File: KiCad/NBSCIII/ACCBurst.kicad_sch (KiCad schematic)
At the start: 56 parts, among them Q901 BC337-25, Q902 BC337-25, Q903 BC337-25, Q910 BC337-25, Q911 BC337-25, Q912 BC337-25, U1 LM324N

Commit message: unrescue Device:D
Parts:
- D901, D902, D930: symbol NBSCIII-rescue:DIODE -> Device:D
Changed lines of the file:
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@@
   (junction (at 238.76 87.63) (diameter 0) (color 0 0 0 0)
   )
+  (junction (at 204.47 129.54) (diameter 0) (color 0 0 0 0)
+  )
+  (junction (at 180.34 113.03) (diameter 0) (color 0 0 0 0)
+  )
+  (junction (at 118.11 25.4) (diameter 0) (color 0 0 0 0)
+  )
+  (junction (at 49.53 105.41) (diameter 0) (color 0 0 0 0)
+  )
+  (junction (at 148.59 129.54) (diameter 0) (color 0 0 0 0)
+  )
+  (junction (at 167.64 87.63) (diameter 0) (color 0 0 0 0)
+  )
+  (junction (at 29.21 129.54) (diameter 0) (color 0 0 0 0)
+  )
   (junction (at 227.33 116.84) (diameter 0) (color 0 0 0 0)
   )
-  (junction (at 204.47 129.54) (diameter 0) (color 0 0 0 0)
-  )
-  (junction (at 180.34 113.03) (diameter 0) (color 0 0 0 0)
-  )
-  (junction (at 118.11 25.4) (diameter 0) (color 0 0 0 0)
-  )
-  (junction (at 49.53 105.41) (diameter 0) (color 0 0 0 0)
-  )
-  (junction (at 148.59 129.54) (diameter 0) (color 0 0 0 0)
-  )
-  (junction (at 167.64 87.63) (diameter 0) (color 0 0 0 0)
-  )
-  (junction (at 29.21 129.54) (diameter 0) (color 0 0 0 0)
-  )
   (junction (at 64.77 25.4) (diameter 0) (color 0 0 0 0)
   )
@@
     (stroke (width 0) (type default) (color 0 0 0 0))
   )
-  (wire (pts (xy 243.84 142.24) (xy 264.16 142.24))
+  (wire (pts (xy 242.57 142.24) (xy 264.16 142.24))
     (stroke (width 0) (type default) (color 0 0 0 0))
   )
@@
     (stroke (width 0) (type default) (color 0 0 0 0))
   )
-  (wire (pts (xy 227.33 106.68) (xy 227.33 105.41))
-    (stroke (width 0) (type default) (color 0 0 0 0))
-  )
   (wire (pts (xy 227.33 105.41) (xy 205.74 105.41))
     (stroke (width 0) (type default) (color 0 0 0 0))
@@
     (stroke (width 0) (type default) (color 0 0 0 0))
   )
-  (wire (pts (xy 102.87 142.24) (xy 233.68 142.24))
+  (wire (pts (xy 102.87 142.24) (xy 234.95 142.24))
     (stroke (width 0) (type default) (color 0 0 0 0))
   )
@@
     (stroke (width 0) (type default) (color 0 0 0 0))
   )
-  (wire (pts (xy 180.34 67.31) (xy 180.34 72.39))
+  (wire (pts (xy 180.34 66.04) (xy 180.34 72.39))
     (stroke (width 0) (type default) (color 0 0 0 0))
   )
@@
     (stroke (width 0) (type default) (color 0 0 0 0))
   )
+  (wire (pts (xy 227.33 105.41) (xy 227.33 107.95))
+    (stroke (width 0) (type default) (color 0 0 0 0))
+  )
   (wire (pts (xy 102.87 129.54) (xy 68.58 129.54))
     (stroke (width 0) (type default) (color 0 0 0 0))
@@
     (stroke (width 0) (type default) (color 0 0 0 0))
   )
-  (wire (pts (xy 180.34 39.37) (xy 180.34 57.15))
+  (wire (pts (xy 180.34 39.37) (xy 180.34 58.42))
     (stroke (width 0) (type default) (color 0 0 0 0))
   )
@@
     (stroke (width 0) (type default) (color 0 0 0 0))
   )
+  (wire (pts (xy 227.33 116.84) (xy 231.14 116.84))
+    (stroke (width 0) (type default) (color 0 0 0 0))
+  )
   (wire (pts (xy 49.53 120.65) (xy 49.53 129.54))
     (stroke (width 0) (type default) (color 0 0 0 0))
@@
     (stroke (width 0) (type default) (color 0 0 0 0))
   )
+  (wire (pts (xy 227.33 115.57) (xy 227.33 116.84))
+    (stroke (width 0) (type default) (color 0 0 0 0))
+  )
   (polyline (pts (xy 22.86 88.9) (xy 22.86 132.08))
     (stroke (width 0) (type default) (color 0 0 0 0))
@@
   )
   (polyline (pts (xy 232.41 147.32) (xy 232.41 86.36))
-    (stroke (width 0) (type default) (color 0 0 0 0))
-  )
-  (wire (pts (xy 227.33 116.84) (xy 231.14 116.84))
     (stroke (width 0) (type default) (color 0 0 0 0))
   )
@@
     (pin "2")
   )
-  (symbol (lib_id "NBSCIII-rescue:DIODE") (at 180.34 62.23 270) (unit 1)
+  (symbol (lib_id "Device:D") (at 180.34 62.23 270) (unit 1)
     (in_bom yes) (on_board yes)
     (property "Reference" "D901" (id 0) (at 182.88 62.23 0)
@@
     (pin "2")
   )
-  (symbol (lib_id "NBSCIII-rescue:DIODE") (at 227.33 111.76 90) (unit 1)
+  (symbol (lib_id "Device:D") (at 227.33 111.76 90) (unit 1)
     (in_bom yes) (on_board yes)
     (property "Reference" "D902" (id 0) (at 224.79 111.76 0)
@@
     (pin "2")
   )
-  (symbol (lib_id "NBSCIII-rescue:DIODE") (at 238.76 142.24 0) (unit 1)
+  (symbol (lib_id "Device:D") (at 238.76 142.24 0) (unit 1)
     (in_bom yes) (on_board yes)
     (property "Reference" "D930" (id 0) (at 238.76 139.7 0)

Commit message: unrescue Device:L_small
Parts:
- L910, L911: symbol NBSCIII-rescue:INDUCTOR -> Device:L_Small
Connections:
- net VIDEO renamed video
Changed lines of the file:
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@@
     (stroke (width 0) (type default) (color 0 0 0 0))
   )
-  (wire (pts (xy 41.91 109.22) (xy 41.91 105.41))
+  (wire (pts (xy 41.91 105.41) (xy 41.91 114.3))
     (stroke (width 0) (type default) (color 0 0 0 0))
   )
@@
     (stroke (width 0) (type default) (color 0 0 0 0))
   )
-  (wire (pts (xy 41.91 129.54) (xy 41.91 124.46))
+  (wire (pts (xy 41.91 119.38) (xy 41.91 129.54))
     (stroke (width 0) (type default) (color 0 0 0 0))
   )
@@
     (stroke (width 0) (type default) (color 0 0 0 0))
   )
-  (wire (pts (xy 185.42 87.63) (xy 185.42 88.9))
+  (wire (pts (xy 185.42 87.63) (xy 185.42 93.98))
     (stroke (width 0) (type default) (color 0 0 0 0))
   )
@@
     (stroke (width 0) (type default) (color 0 0 0 0))
   )
-  (wire (pts (xy 185.42 104.14) (xy 185.42 105.41))
+  (wire (pts (xy 185.42 99.06) (xy 185.42 105.41))
     (stroke (width 0) (type default) (color 0 0 0 0))
   )
@@
     (effects (font (size 1.524 1.524)) (justify right))
   )
-  (hierarchical_label "VIDEO" (shape input) (at 22.86 92.71 180)
+  (hierarchical_label "video" (shape input) (at 22.86 92.71 180)
     (effects (font (size 1.524 1.524)) (justify right))
   )
@@
     (pin "2")
   )
-  (symbol (lib_id "NBSCIII-rescue:INDUCTOR") (at 41.91 116.84 0) (unit 1)
+  (symbol (lib_id "Device:L_Small") (at 41.91 116.84 0) (unit 1)
     (in_bom yes) (on_board yes)
     (property "Reference" "L910" (id 0) (at 40.64 116.84 90)
@@
     (pin "2")
   )
-  (symbol (lib_id "NBSCIII-rescue:INDUCTOR") (at 185.42 96.52 0) (unit 1)
+  (symbol (lib_id "Device:L_Small") (at 185.42 96.52 0) (unit 1)
     (in_bom yes) (on_board yes)
     (property "Reference" "L911" (id 0) (at 184.15 96.52 90)

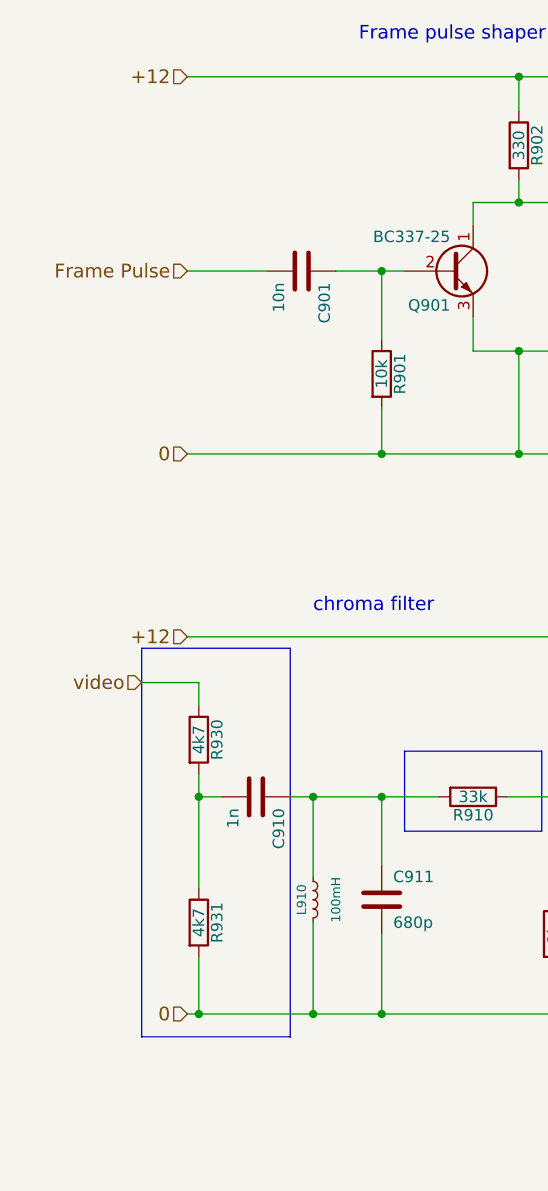
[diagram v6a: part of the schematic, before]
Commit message: Simplify power distribution and make global
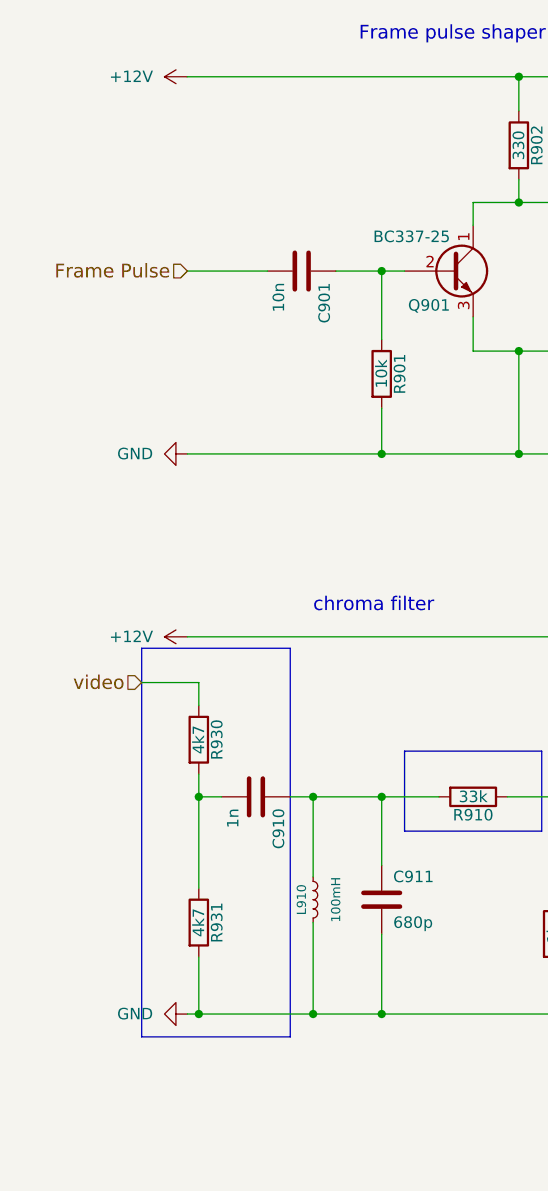
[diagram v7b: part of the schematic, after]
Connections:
- net +12 renamed +12V
- net 0 renamed GND
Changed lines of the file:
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@@
     (effects (font (size 1.524 1.524)) (justify left bottom))
-  )
-  (hierarchical_label "+12" (shape input) (at 27.94 87.63 180)
-    (effects (font (size 1.524 1.524)) (justify right))
   )
   (hierarchical_label "C" (shape output) (at 162.56 135.89 0)
     (effects (font (size 1.524 1.524)) (justify left))
   )
-  (hierarchical_label "0" (shape input) (at 27.94 129.54 180)
-    (effects (font (size 1.524 1.524)) (justify right))
-  )
   (hierarchical_label "Frame Pulse" (shape input) (at 27.94 46.99 180)
     (effects (font (size 1.524 1.524)) (justify right))
   )
-  (hierarchical_label "+12" (shape input) (at 27.94 25.4 180)
-    (effects (font (size 1.524 1.524)) (justify right))
-  )
   (hierarchical_label "BURST" (shape output) (at 231.14 105.41 0)
     (effects (font (size 1.524 1.524)) (justify left))
-  )
-  (hierarchical_label "0" (shape input) (at 27.94 67.31 180)
-    (effects (font (size 1.524 1.524)) (justify right))
   )
   (hierarchical_label "video" (shape input) (at 22.86 92.71 180)
@@
     (pin "2")
   )
+  (symbol (lib_id "power:+12V") (at 27.94 87.63 90) (unit 1)
+    (in_bom yes) (on_board yes) (fields_autoplaced)
+    (property "Reference" "#PWR0121" (id 0) (at 31.75 87.63 0)
+      (effects (font (size 1.27 1.27)) hide)
+    )
+    (property "Value" "+12V" (id 1) (at 24.13 87.6299 90)
+      (effects (font (size 1.27 1.27)) (justify left))
+    )
+    (property "Footprint" "" (id 2) (at 27.94 87.63 0)
+      (effects (font (size 1.27 1.27)) hide)
+    )
+    (property "Datasheet" "" (id 3) (at 27.94 87.63 0)
+      (effects (font (size 1.27 1.27)) hide)
+    )
+    (pin "1")
+  )
+  (symbol (lib_id "power:GND") (at 27.94 129.54 270) (unit 1)
+    (in_bom yes) (on_board yes) (fields_autoplaced)
+    (property "Reference" "#PWR0120" (id 0) (at 21.59 129.54 0)
+      (effects (font (size 1.27 1.27)) hide)
+    )
+    (property "Value" "GND" (id 1) (at 24.13 129.5399 90)
+      (effects (font (size 1.27 1.27)) (justify right))
+    )
+    (property "Footprint" "" (id 2) (at 27.94 129.54 0)
+      (effects (font (size 1.27 1.27)) hide)
+    )
+    (property "Datasheet" "" (id 3) (at 27.94 129.54 0)
+      (effects (font (size 1.27 1.27)) hide)
+    )
+    (pin "1")
+  )
+  (symbol (lib_id "power:+12V") (at 27.94 25.4 90) (unit 1)
+    (in_bom yes) (on_board yes) (fields_autoplaced)
+    (property "Reference" "#PWR0119" (id 0) (at 31.75 25.4 0)
+      (effects (font (size 1.27 1.27)) hide)
+    )
+    (property "Value" "+12V" (id 1) (at 24.13 25.3999 90)
+      (effects (font (size 1.27 1.27)) (justify left))
+    )
+    (property "Footprint" "" (id 2) (at 27.94 25.4 0)
+      (effects (font (size 1.27 1.27)) hide)
+    )
+    (property "Datasheet" "" (id 3) (at 27.94 25.4 0)
+      (effects (font (size 1.27 1.27)) hide)
+    )
+    (pin "1")
+  )
+  (symbol (lib_id "power:GND") (at 27.94 67.31 270) (unit 1)
+    (in_bom yes) (on_board yes) (fields_autoplaced)
+    (property "Reference" "#PWR0118" (id 0) (at 21.59 67.31 0)
+      (effects (font (size 1.27 1.27)) hide)
+    )
+    (property "Value" "GND" (id 1) (at 24.13 67.3099 90)
+      (effects (font (size 1.27 1.27)) (justify right))
+    )
+    (property "Footprint" "" (id 2) (at 27.94 67.31 0)
+      (effects (font (size 1.27 1.27)) hide)
+    )
+    (property "Datasheet" "" (id 3) (at 27.94 67.31 0)
+      (effects (font (size 1.27 1.27)) hide)
+    )
+    (pin "1")
+  )
 )

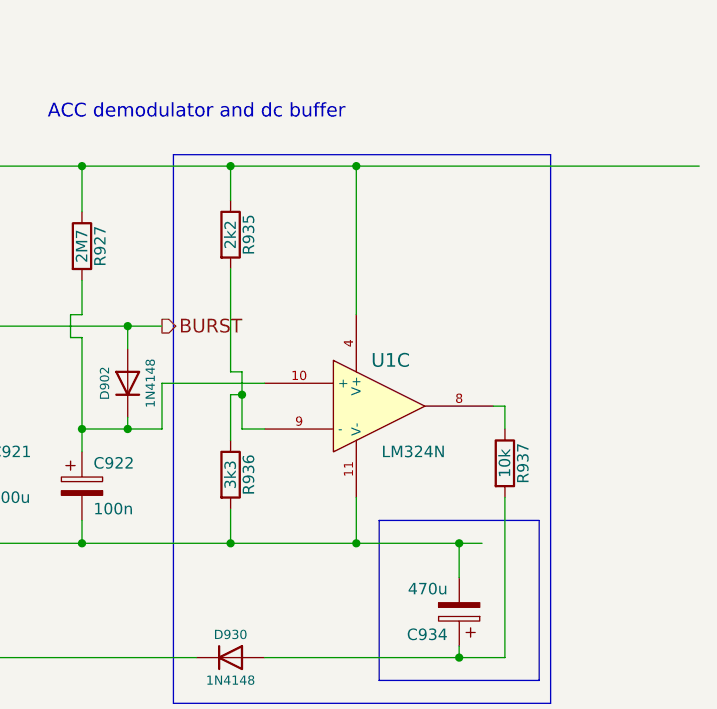
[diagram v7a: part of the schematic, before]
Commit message: derescue lm324
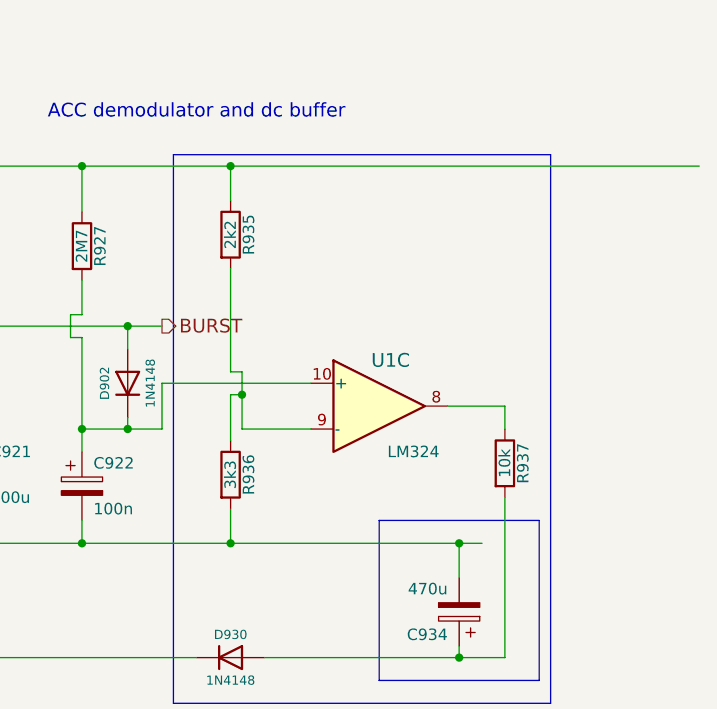
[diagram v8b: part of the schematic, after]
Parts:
- U1: value LM324N -> LM324; symbol NBSCIII-rescue:LM324N -> Amplifier_Operational:LM324
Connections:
- net +12V: no longer U1.4 (V+)
- net GND: no longer U1.11 (V-)
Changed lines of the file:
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@@
   (junction (at 210.82 129.54) (diameter 0) (color 0 0 0 0)
   )
-  (junction (at 252.73 87.63) (diameter 0) (color 0 0 0 0)
-  )
   (junction (at 204.47 114.3) (diameter 0) (color 0 0 0 0)
   )
@@
   (junction (at 130.81 102.87) (diameter 0) (color 0 0 0 0)
   )
-  (junction (at 252.73 129.54) (diameter 0) (color 0 0 0 0)
-  )
   (junction (at 146.05 104.14) (diameter 0) (color 0 0 0 0)
   )
@@
     (stroke (width 0) (type default) (color 0 0 0 0))
   )
-  (wire (pts (xy 231.14 111.76) (xy 242.57 111.76))
-    (stroke (width 0) (type default) (color 0 0 0 0))
-  )
   (wire (pts (xy 41.91 105.41) (xy 49.53 105.41))
     (stroke (width 0) (type default) (color 0 0 0 0))
@@
     (stroke (width 0) (type default) (color 0 0 0 0))
   )
-  (wire (pts (xy 267.97 114.3) (xy 269.24 114.3))
+  (wire (pts (xy 262.89 114.3) (xy 269.24 114.3))
     (stroke (width 0) (type default) (color 0 0 0 0))
   )
@@
     (stroke (width 0) (type default) (color 0 0 0 0))
   )
-  (wire (pts (xy 252.73 129.54) (xy 238.76 129.54))
+  (wire (pts (xy 238.76 129.54) (xy 264.16 129.54))
     (stroke (width 0) (type default) (color 0 0 0 0))
   )
@@
     (stroke (width 0) (type default) (color 0 0 0 0))
   )
-  (wire (pts (xy 264.16 129.54) (xy 252.73 129.54))
-    (stroke (width 0) (type default) (color 0 0 0 0))
-  )
   (wire (pts (xy 180.34 111.76) (xy 176.53 111.76))
     (stroke (width 0) (type default) (color 0 0 0 0))
@@
     (stroke (width 0) (type default) (color 0 0 0 0))
   )
+  (wire (pts (xy 240.03 116.84) (xy 247.65 116.84))
+    (stroke (width 0) (type default) (color 0 0 0 0))
+  )
   (polyline (pts (xy 115.57 30.48) (xy 77.47 30.48))
     (stroke (width 0) (type default) (color 0 0 0 0))
   )
+  (wire (pts (xy 231.14 111.76) (xy 247.65 111.76))
+    (stroke (width 0) (type default) (color 0 0 0 0))
+  )
   (wire (pts (xy 156.21 104.14) (xy 158.75 104.14))
     (stroke (width 0) (type default) (color 0 0 0 0))
@@
     (stroke (width 0) (type default) (color 0 0 0 0))
   )
-  (wire (pts (xy 242.57 116.84) (xy 240.03 116.84))
-    (stroke (width 0) (type default) (color 0 0 0 0))
-  )
   (wire (pts (xy 264.16 129.54) (xy 264.16 133.35))
     (stroke (width 0) (type default) (color 0 0 0 0))
@@
     (stroke (width 0) (type default) (color 0 0 0 0))
   )
-  (wire (pts (xy 252.73 87.63) (xy 290.83 87.63))
+  (wire (pts (xy 238.76 87.63) (xy 290.83 87.63))
     (stroke (width 0) (type default) (color 0 0 0 0))
   )
@@
     (stroke (width 0) (type default) (color 0 0 0 0))
   )
-  (wire (pts (xy 252.73 124.46) (xy 252.73 129.54))
-    (stroke (width 0) (type default) (color 0 0 0 0))
-  )
   (wire (pts (xy 118.11 52.07) (xy 118.11 67.31))
     (stroke (width 0) (type default) (color 0 0 0 0))
@@
     (stroke (width 0) (type default) (color 0 0 0 0))
   )
-  (wire (pts (xy 252.73 104.14) (xy 252.73 87.63))
-    (stroke (width 0) (type default) (color 0 0 0 0))
-  )
   (wire (pts (xy 85.09 130.81) (xy 85.09 128.27))
     (stroke (width 0) (type default) (color 0 0 0 0))
@@
   )
   (wire (pts (xy 156.21 113.03) (xy 162.56 113.03))
-    (stroke (width 0) (type default) (color 0 0 0 0))
-  )
-  (wire (pts (xy 238.76 87.63) (xy 252.73 87.63))
     (stroke (width 0) (type default) (color 0 0 0 0))
   )
@@
     (pin "2")
   )
-  (symbol (lib_id "NBSCIII-rescue:LM324N") (at 255.27 114.3 0) (unit 3)
+  (symbol (lib_id "Amplifier_Operational:LM324") (at 255.27 114.3 0) (unit 3)
     (in_bom yes) (on_board yes)
     (property "Reference" "U1" (id 0) (at 256.54 109.22 0)
       (effects (font (size 1.524 1.524)))
     )
-    (property "Value" "LM324N" (id 1) (at 259.08 119.38 0))
+    (property "Value" "LM324" (id 1) (at 259.08 119.38 0))
     (property "Footprint" "" (id 2) (at 255.27 114.3 0)
       (effects (font (size 1.27 1.27)) hide)
@@
       (effects (font (size 1.27 1.27)) hide)
     )
-    (pin "11")
-    (pin "4")
     (pin "1")
     (pin "2")
@@
     (pin "13")
     (pin "14")
+    (pin "11")
+    (pin "4")
   )
   (symbol (lib_id "Device:R") (at 29.21 119.38 0) (unit 1)
